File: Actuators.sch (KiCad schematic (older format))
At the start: 14 parts, among them J1 SERVO PWR, M1 Motor_Servo, M2 Motor_Servo, M3 Pump 1, M4 Pump 2, U6 DRV8847PWR

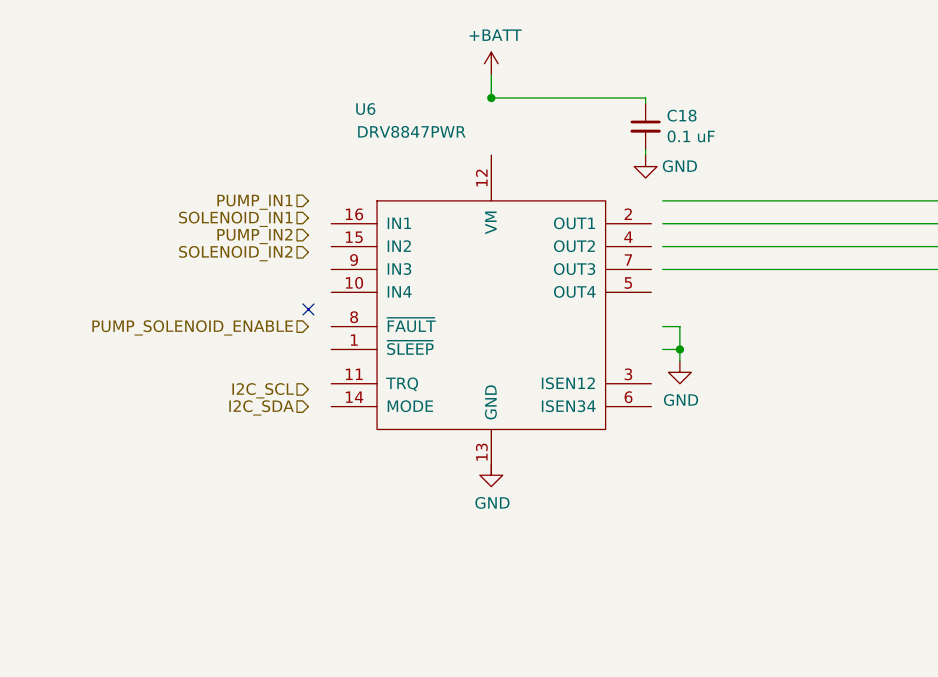
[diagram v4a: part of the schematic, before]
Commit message: Switch to SPI, fixed sensor and motor driver symbols.
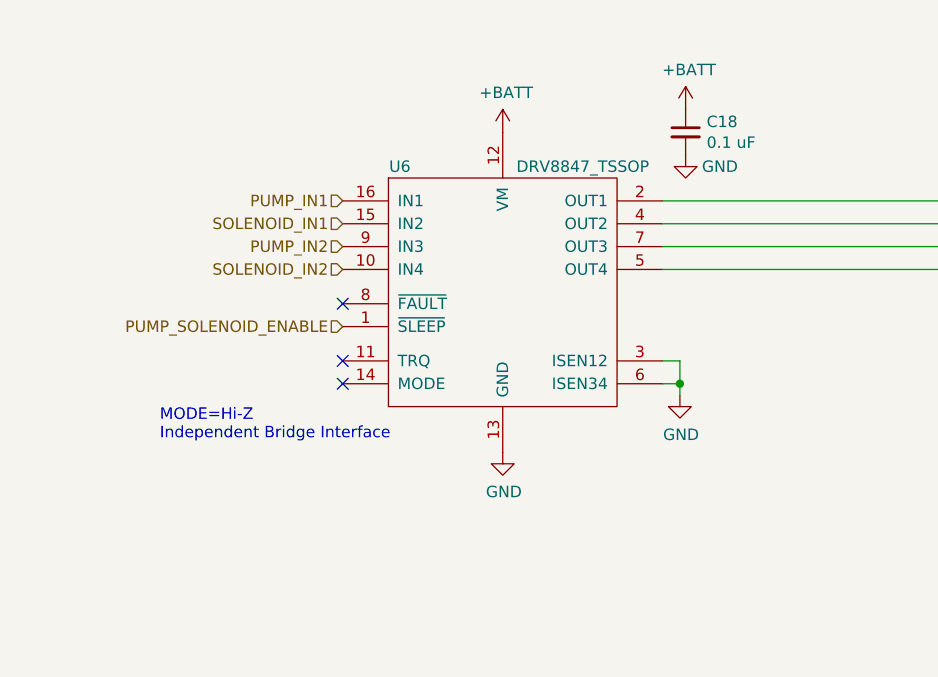
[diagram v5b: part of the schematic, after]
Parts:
- U6: value DRV8847PWR -> DRV8847_TSSOP; Digikey 296-53425-1-ND -> (none)
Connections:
- net labels removed: I2C_SCL, I2C_SDA
- wire segments 48 -> 44
- no-connect marks 1 -> 3
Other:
- note added: "MODE=Hi-Z\nIndependent Bridge Interface"
- moved on the sheet: C18
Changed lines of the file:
@@
 Comment4 ""
 $EndDescr
-Text HLabel 3700 2650 0    50   Input ~ 0
+Text HLabel 3850 2650 0    50   Input ~ 0
 PUMP_IN1
-Text HLabel 3700 2800 0    50   Input ~ 0
+Text HLabel 3850 2850 0    50   Input ~ 0
 PUMP_IN2
-Text HLabel 3700 3200 0    50   Input ~ 0
+Text HLabel 3850 3200 0    50   Input ~ 0
 PUMP_SOLENOID_ENABLE
 Text HLabel 4500 5250 0    50   Input ~ 0
@@
 Text HLabel 4500 5800 0    50   Input ~ 0
 SERVO2
-Text HLabel 3700 3550 0    50   Input ~ 0
-I2C_SDA
-Text HLabel 3700 3475 0    50   Input ~ 0
-I2C_SCL
-NoConn ~ 3700 3125
-$Comp
-L power:GND #PWR035
+NoConn ~ 3850 3100
+$Comp
+L power:GND #PWR037
 U 1 1 5E239CA6
-P 4500 3800
-F 0 "#PWR035" H 4500 3550 50  0001 C CNN
-F 1 "GND" H 4505 3627 50  0000 C CNN
-F 2 "" H 4500 3800 50  0001 C CNN
-F 3 "" H 4500 3800 50  0001 C CNN
-	1    4500 3800
-	1    0    0    -1
-$EndComp
-$Comp
-L power:GND #PWR039
+P 4550 3750
+F 0 "#PWR037" H 4550 3500 50  0001 C CNN
+F 1 "GND" H 4555 3577 50  0000 C CNN
+F 2 "" H 4550 3750 50  0001 C CNN
+F 3 "" H 4550 3750 50  0001 C CNN
+	1    4550 3750
+	1    0    0    -1
+$EndComp
+$Comp
+L power:GND #PWR040
 U 1 1 5E260916
-P 5325 3350
-F 0 "#PWR039" H 5325 3100 50  0001 C CNN
-F 1 "GND" H 5330 3177 50  0000 C CNN
-F 2 "" H 5325 3350 50  0001 C CNN
-F 3 "" H 5325 3350 50  0001 C CNN
-	1    5325 3350
-	1    0    0    -1
-$EndComp
-Wire Wire Line
-	5250 3300 5325 3300
-Wire Wire Line
-	5250 3200 5325 3200
-Wire Wire Line
-	5325 3200 5325 3300
-Connection ~ 5325 3300
-Wire Wire Line
-	5325 3300 5325 3350
-Text HLabel 3700 2875 0    50   Input ~ 0
+P 5325 3500
+F 0 "#PWR040" H 5325 3250 50  0001 C CNN
+F 1 "GND" H 5330 3327 50  0000 C CNN
+F 2 "" H 5325 3500 50  0001 C CNN
+F 3 "" H 5325 3500 50  0001 C CNN
+	1    5325 3500
+	1    0    0    -1
+$EndComp
+Wire Wire Line
+	5250 3450 5325 3450
+Wire Wire Line
+	5250 3350 5325 3350
+Wire Wire Line
+	5325 3350 5325 3450
+Connection ~ 5325 3450
+Wire Wire Line
+	5325 3450 5325 3500
+Text HLabel 3850 2950 0    50   Input ~ 0
 SOLENOID_IN2
-$Comp
-L Device:C_Small C18
-U 1 1 5E2FBBF2
-P 5175 2325
-F 0 "C18" H 5267 2371 50  0000 L CNN
-F 1 "0.1 uF" H 5267 2280 50  0000 L CNN
-F 2 "" H 5175 2325 50  0001 C CNN
-F 3 "~" H 5175 2325 50  0001 C CNN
-	1    5175 2325
-	1    0    0    -1
-$EndComp
-$Comp
-L power:GND #PWR038
-U 1 1 5E2FC82D
-P 5175 2450
-F 0 "#PWR038" H 5175 2200 50  0001 C CNN
-F 1 "GND" H 5325 2400 50  0000 C CNN
-F 2 "" H 5175 2450 50  0001 C CNN
-F 3 "" H 5175 2450 50  0001 C CNN
-	1    5175 2450
-	1    0    0    -1
-$EndComp
-Wire Wire Line
-	5175 2225 5175 2200
-Wire Wire Line
-	4500 2200 5175 2200
-Wire Wire Line
-	5175 2425 5175 2450
 $Comp
 L Motor:Motor_Servo M1
@@
 	1    0    0    -1
 $EndComp
-$Comp
-L _power:DRV8847_TSSOP U6
-U 1 1 5E23D2B5
-P 4500 3150
-F 0 "U6" H 3950 4050 50  0000 C CNN
-F 1 "DRV8847PWR" H 4150 3950 50  0000 C CNN
-F 2 "" H 4500 3150 50  0001 C CNN
-F 3 "" H 4500 3150 50  0001 C CNN
-F 4 "296-53425-1-ND" H 4500 3150 50  0001 C CNN "Digikey"
-	1    4500 3150
-	1    0    0    -1
-$EndComp
-Text HLabel 3700 2725 0    50   Input ~ 0
+Text HLabel 3850 2750 0    50   Input ~ 0
 SOLENOID_IN1
 $Comp
@@
 P 3350 5650
 AR Path="/5E3A79FB" Ref="#PWR?"  Part="1"
-AR Path="/5E1FB153/5E3A79FB" Ref="#PWR033"  Part="1"
-F 0 "#PWR033" H 3350 5400 50  0001 C CNN
+AR Path="/5E1FB153/5E3A79FB" Ref="#PWR035"  Part="1"
+F 0 "#PWR035" H 3350 5400 50  0001 C CNN
 F 1 "GND" H 3355 5477 50  0000 C CNN
 F 2 "" H 3350 5650 50  0001 C CNN
@@
 P 4700 5450
 AR Path="/5E3D17A5" Ref="#PWR?"  Part="1"
-AR Path="/5E1FB153/5E3D17A5" Ref="#PWR036"  Part="1"
-F 0 "#PWR036" H 4700 5200 50  0001 C CNN
+AR Path="/5E1FB153/5E3D17A5" Ref="#PWR038"  Part="1"
+F 0 "#PWR038" H 4700 5200 50  0001 C CNN
 F 1 "GND" H 4705 5277 50  0000 C CNN
 F 2 "" H 4700 5450 50  0001 C CNN
@@
 P 4700 6000
 AR Path="/5E3D4696" Ref="#PWR?"  Part="1"
-AR Path="/5E1FB153/5E3D4696" Ref="#PWR037"  Part="1"
-F 0 "#PWR037" H 4700 5750 50  0001 C CNN
+AR Path="/5E1FB153/5E3D4696" Ref="#PWR039"  Part="1"
+F 0 "#PWR039" H 4700 5750 50  0001 C CNN
 F 1 "GND" H 4705 5827 50  0000 C CNN
 F 2 "" H 4700 6000 50  0001 C CNN
@@
 	4700 5250 4500 5250
 $Comp
-L power:+BATT #PWR034
+L power:+BATT #PWR036
 U 1 1 5E3DDDE9
-P 4500 2100
-F 0 "#PWR034" H 4500 1950 50  0001 C CNN
-F 1 "+BATT" H 4515 2273 50  0000 C CNN
-F 2 "" H 4500 2100 50  0001 C CNN
-F 3 "" H 4500 2100 50  0001 C CNN
-	1    4500 2100
-	1    0    0    -1
-$EndComp
-Wire Wire Line
-	4500 2200 4500 2100
-Connection ~ 4500 2200
+P 4550 2350
+F 0 "#PWR036" H 4550 2200 50  0001 C CNN
+F 1 "+BATT" H 4565 2523 50  0000 C CNN
+F 2 "" H 4550 2350 50  0001 C CNN
+F 3 "" H 4550 2350 50  0001 C CNN
+	1    4550 2350
+	1    0    0    -1
+$EndComp
 $Comp
 L Motor:Motor_DC M3
@@
 Text Notes 7600 4250 0    50   ~ 0
 Actuator 2\n(1A max)
+$Comp
+L _power:DRV8847_TSSOP U6
+U 1 1 5E3FBC0B
+P 4550 3050
+F 0 "U6" H 4100 3600 50  0000 C CNN
+F 1 "DRV8847_TSSOP" H 4900 3600 50  0000 C CNN
+F 2 "" H 4550 3000 50  0001 C CNN
+F 3 "http://www.ti.com/lit/ds/symlink/drv8847.pdf" H 4550 3000 50  0001 C CNN
+	1    4550 3050
+	1    0    0    -1
+$EndComp
+$Comp
+L power:GND #PWR041
+U 1 1 5E2FC82D
+P 5350 2450
+F 0 "#PWR041" H 5350 2200 50  0001 C CNN
+F 1 "GND" H 5500 2400 50  0000 C CNN
+F 2 "" H 5350 2450 50  0001 C CNN
+F 3 "" H 5350 2450 50  0001 C CNN
+	1    5350 2450
+	1    0    0    -1
+$EndComp
+$Comp
+L Device:C_Small C18
+U 1 1 5E2FBBF2
+P 5350 2350
+F 0 "C18" H 5442 2396 50  0000 L CNN
+F 1 "0.1 uF" H 5442 2305 50  0000 L CNN
+F 2 "" H 5350 2350 50  0001 C CNN
+F 3 "~" H 5350 2350 50  0001 C CNN
+	1    5350 2350
+	1    0    0    -1
+$EndComp
+NoConn ~ 3850 3450
+NoConn ~ 3850 3350
+Text Notes 3050 3700 0    50   ~ 0
+MODE=Hi-Z\nIndependent Bridge Interface
+$Comp
+L power:+BATT #PWR?
+U 1 1 5E4403AD
+P 5350 2250
+F 0 "#PWR?" H 5350 2100 50  0001 C CNN
+F 1 "+BATT" H 5365 2423 50  0000 C CNN
+F 2 "" H 5350 2250 50  0001 C CNN
+F 3 "" H 5350 2250 50  0001 C CNN
+	1    5350 2250
+	1    0    0    -1
+$EndComp
 $EndSCHEMATC

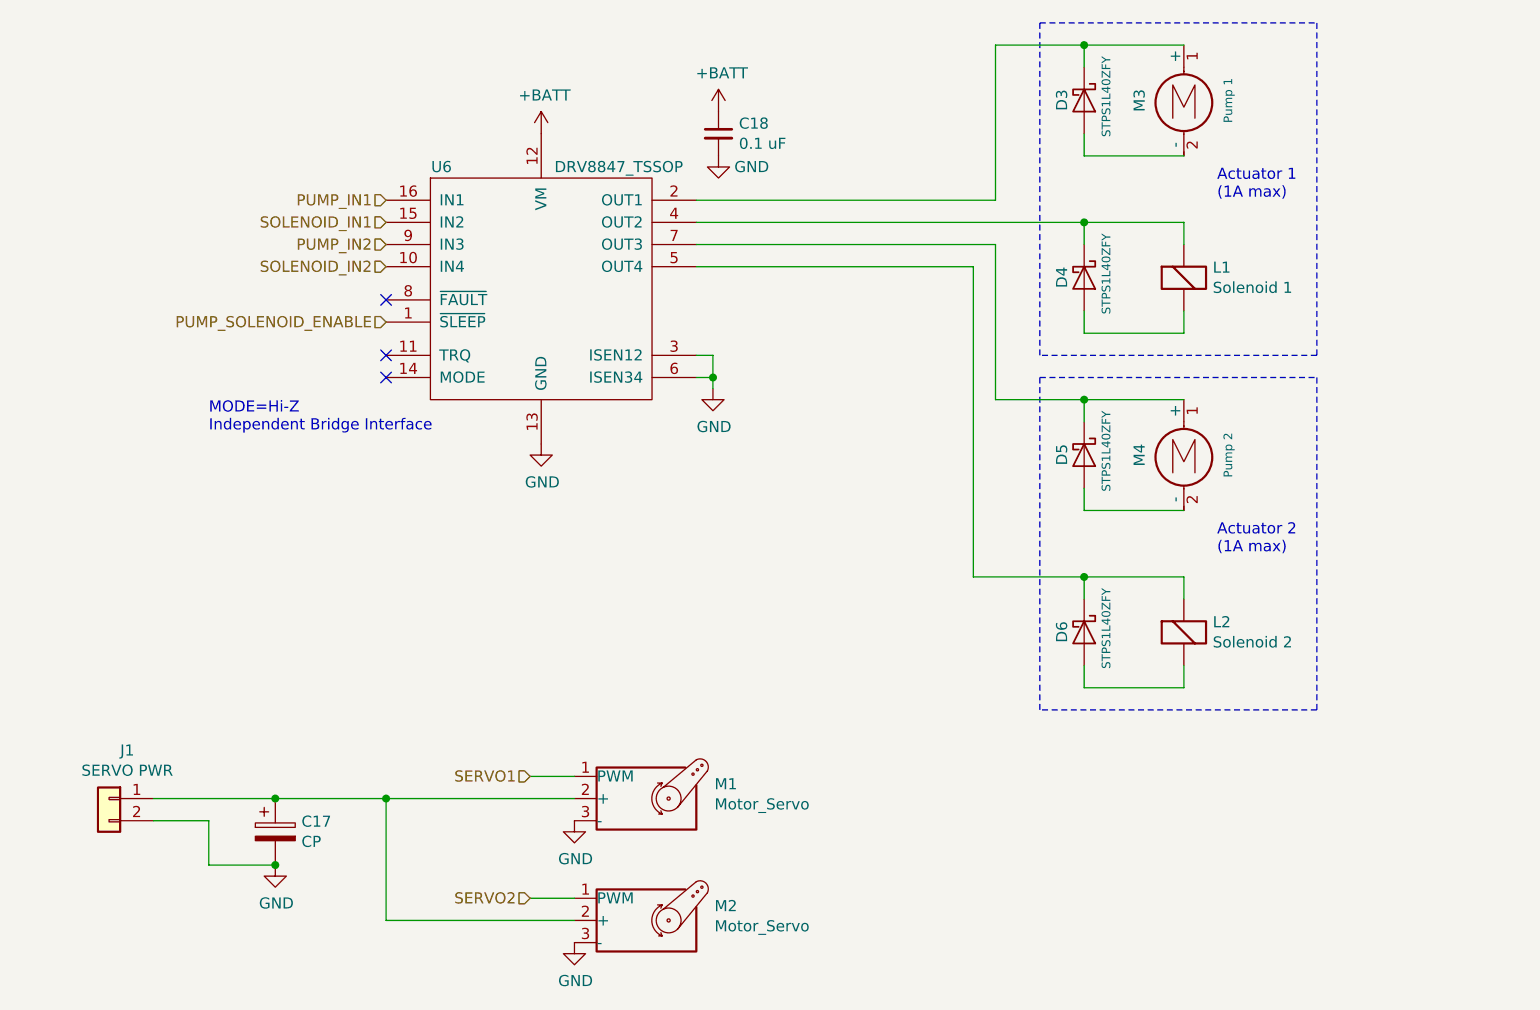
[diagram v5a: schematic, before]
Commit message: Work on footprint assignment
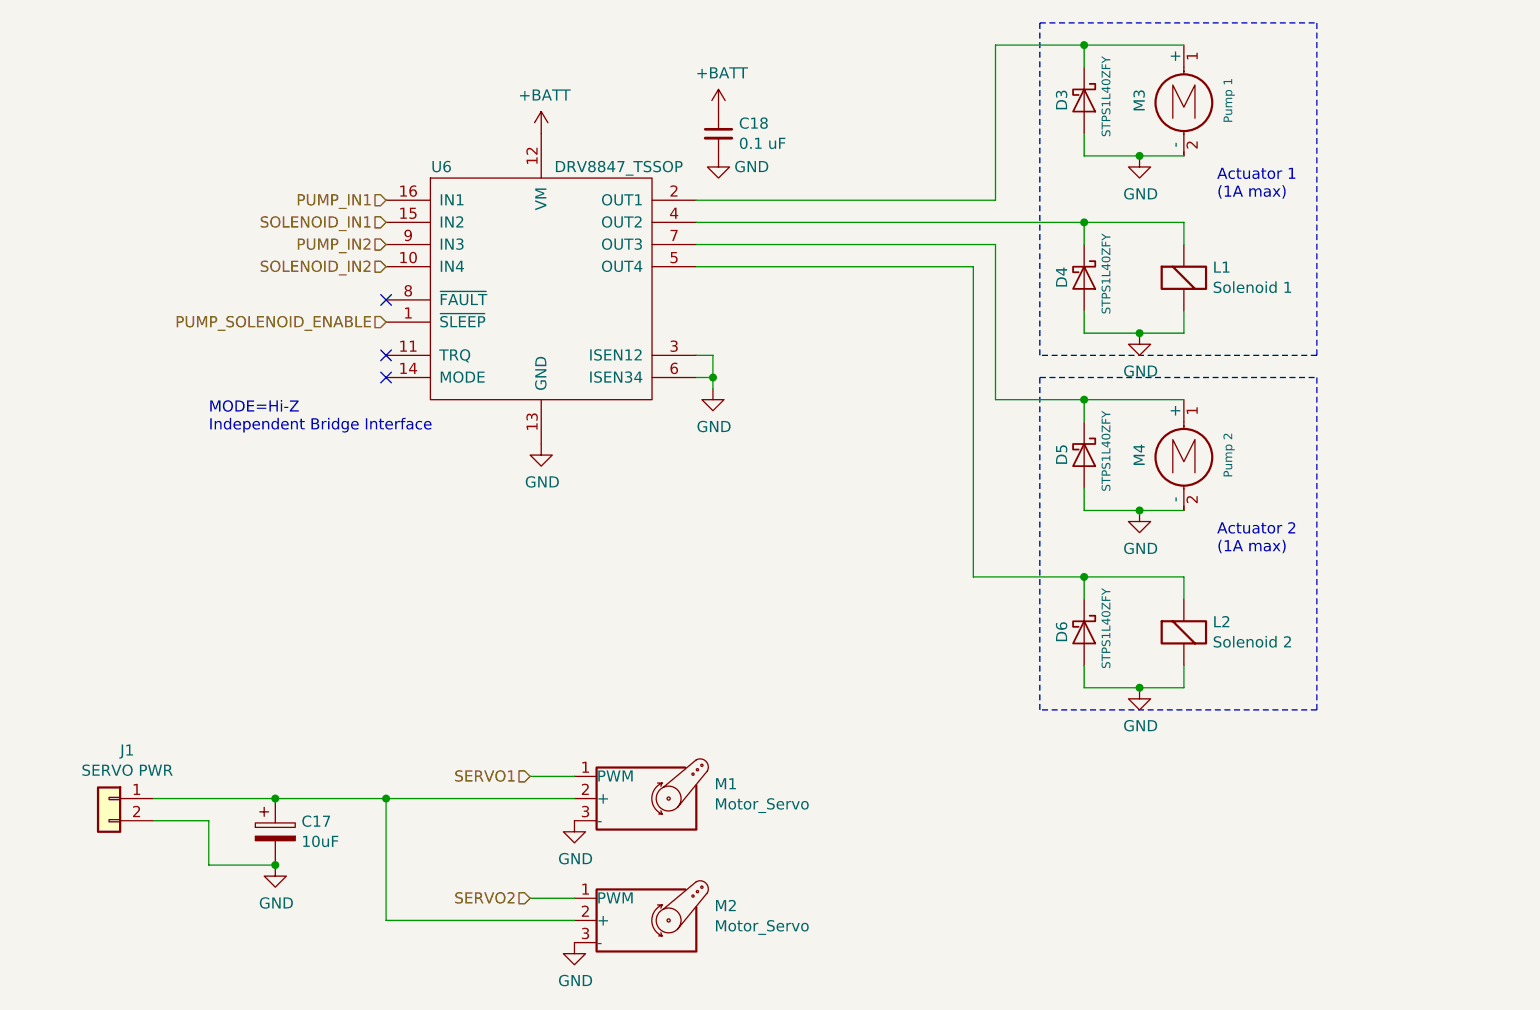
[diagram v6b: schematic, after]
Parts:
- C17: value CP -> 10uF
- C18: footprint (none) -> Capacitor_SMD:C_0603_1608Metric
- M1, M2: footprint (none) -> Connector_PinHeader_2.54mm:PinHeader_1x03_P2.54mm_Horizontal
- U6: footprint (none) -> Package_SO:TSSOP-16_4.4x5mm_P0.65mm
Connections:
- net GND: now also D3.2 (A), D4.2 (A), D5.2 (A), D6.2 (A), L1.2 (+), L2.2 (+), M3.2 (-), M4.2 (-)
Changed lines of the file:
@@
 F 0 "M1" H 5332 5415 50  0000 L CNN
 F 1 "Motor_Servo" H 5332 5324 50  0000 L CNN
-F 2 "" H 5000 5160 50  0001 C CNN
+F 2 "Connector_PinHeader_2.54mm:PinHeader_1x03_P2.54mm_Horizontal" H 5000 5160 50  0001 C CNN
 F 3 "http://forums.parallax.com/uploads/attachments/46831/74481.png" H 5000 5160 50  0001 C CNN
 	1    5000 5350
@@
 F 0 "M2" H 5332 5965 50  0000 L CNN
 F 1 "Motor_Servo" H 5332 5874 50  0000 L CNN
-F 2 "" H 5000 5710 50  0001 C CNN
+F 2 "Connector_PinHeader_2.54mm:PinHeader_1x03_P2.54mm_Horizontal" H 5000 5710 50  0001 C CNN
 F 3 "http://forums.parallax.com/uploads/attachments/46831/74481.png" H 5000 5710 50  0001 C CNN
 	1    5000 5900
@@
 AR Path="/5E1FB153/5E3A79F5" Ref="C17"  Part="1"
 F 0 "C17" H 3468 5546 50  0000 L CNN
-F 1 "CP" H 3468 5455 50  0000 L CNN
+F 1 "10uF" H 3468 5455 50  0000 L CNN
 F 2 "" H 3388 5350 50  0001 C CNN
 F 3 "~" H 3350 5500 50  0001 C CNN
@@
 	7000 2350 7000 2450
 Wire Wire Line
-	7000 2450 7450 2450
+	7000 2450 7250 2450
 Wire Wire Line
 	7000 3650 7000 3550
@@
 	7000 3950 7000 4050
 Wire Wire Line
-	7000 4050 7450 4050
+	7000 4050 7250 4050
 Wire Wire Line
 	7000 4450 7000 4350
@@
 	7000 4750 7000 4850
 Wire Wire Line
-	7000 4850 7450 4850
+	7000 4850 7250 4850
 $Comp
 L Device:D_Schottky D3
@@
 	7000 3150 7000 3250
 Wire Wire Line
-	7000 3250 7450 3250
-Wire Wire Line
 	7000 2750 7450 2750
 Wire Wire Line
@@
 F 0 "U6" H 4100 3600 50  0000 C CNN
 F 1 "DRV8847_TSSOP" H 4900 3600 50  0000 C CNN
-F 2 "" H 4550 3000 50  0001 C CNN
+F 2 "Package_SO:TSSOP-16_4.4x5mm_P0.65mm" H 4550 3000 50  0001 C CNN
 F 3 "http://www.ti.com/lit/ds/symlink/drv8847.pdf" H 4550 3000 50  0001 C CNN
 	1    4550 3050
@@
 F 0 "C18" H 5442 2396 50  0000 L CNN
 F 1 "0.1 uF" H 5442 2305 50  0000 L CNN
-F 2 "" H 5350 2350 50  0001 C CNN
+F 2 "Capacitor_SMD:C_0603_1608Metric" H 5350 2350 50  0001 C CNN
 F 3 "~" H 5350 2350 50  0001 C CNN
 	1    5350 2350
@@
 MODE=Hi-Z\nIndependent Bridge Interface
 $Comp
-L power:+BATT #PWR?
+L power:+BATT #PWR0101
 U 1 1 5E4403AD
 P 5350 2250
-F 0 "#PWR?" H 5350 2100 50  0001 C CNN
+F 0 "#PWR0101" H 5350 2100 50  0001 C CNN
 F 1 "+BATT" H 5365 2423 50  0000 C CNN
 F 2 "" H 5350 2250 50  0001 C CNN
@@
 	1    0    0    -1
 $EndComp
+$Comp
+L power:GND #PWR0102
+U 1 1 5E3F7C81
+P 7250 2450
+F 0 "#PWR0102" H 7250 2200 50  0001 C CNN
+F 1 "GND" H 7255 2277 50  0000 C CNN
+F 2 "" H 7250 2450 50  0001 C CNN
+F 3 "" H 7250 2450 50  0001 C CNN
+	1    7250 2450
+	1    0    0    -1
+$EndComp
+Connection ~ 7250 2450
+Wire Wire Line
+	7250 2450 7450 2450
+Wire Wire Line
+	7000 3250 7250 3250
+$Comp
+L power:GND #PWR0103
+U 1 1 5E3F96C2
+P 7250 3250
+F 0 "#PWR0103" H 7250 3000 50  0001 C CNN
+F 1 "GND" H 7255 3077 50  0000 C CNN
+F 2 "" H 7250 3250 50  0001 C CNN
+F 3 "" H 7250 3250 50  0001 C CNN
+	1    7250 3250
+	1    0    0    -1
+$EndComp
+Connection ~ 7250 3250
+Wire Wire Line
+	7250 3250 7450 3250
+$Comp
+L power:GND #PWR0104
+U 1 1 5E3F9BB4
+P 7250 4050
+F 0 "#PWR0104" H 7250 3800 50  0001 C CNN
+F 1 "GND" H 7255 3877 50  0000 C CNN
+F 2 "" H 7250 4050 50  0001 C CNN
+F 3 "" H 7250 4050 50  0001 C CNN
+	1    7250 4050
+	1    0    0    -1
+$EndComp
+Connection ~ 7250 4050
+Wire Wire Line
+	7250 4050 7450 4050
+$Comp
+L power:GND #PWR0105
+U 1 1 5E3FA1D8
+P 7250 4850
+F 0 "#PWR0105" H 7250 4600 50  0001 C CNN
+F 1 "GND" H 7255 4677 50  0000 C CNN
+F 2 "" H 7250 4850 50  0001 C CNN
+F 3 "" H 7250 4850 50  0001 C CNN
+	1    7250 4850
+	1    0    0    -1
+$EndComp
+Connection ~ 7250 4850
+Wire Wire Line
+	7250 4850 7450 4850
 $EndSCHEMATC

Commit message: Review update
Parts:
- added C19: 22uF, symbol Device:CP
- added R2: 10k, symbol Device:R_Small
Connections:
- net +BATT: now also C19.1
- net GND: now also U6.11 (TRQ), C19.2, R2.2
- net PUMP_SOLENOID_ENABLE: now also R2.1
- no-connect marks 3 -> 2
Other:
- note added: "MODE=Hi-Z: Independent Bridge Interface\nTRQ=0: Full current"
- note added: "≥16V"
- note removed: "MODE=Hi-Z\nIndependent Bridge Interface"
- moved on the sheet: C18, D5, D6, L2, M4

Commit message: Input range note, rough footprint assignment
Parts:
- C17: footprint (none) -> Capacitor_SMD:C_1206_3216Metric
- C19: footprint (none) -> Capacitor_THT:CP_Radial_D6.3mm_P2.50mm
- J1, L1, L2, M3, M4: footprint (none) -> Connector_PinHeader_2.54mm:PinHeader_1x02_P2.54mm_Vertical
- R2: footprint (none) -> Resistor_SMD:R_0603_1608Metric
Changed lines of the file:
@@
 F 0 "C17" H 3468 5546 50  0000 L CNN
 F 1 "10uF" H 3468 5455 50  0000 L CNN
-F 2 "" H 3388 5350 50  0001 C CNN
+F 2 "Capacitor_SMD:C_1206_3216Metric" H 3388 5350 50  0001 C CNN
 F 3 "~" H 3350 5500 50  0001 C CNN
 	1    3350 5500
@@
 F 0 "J1" H 2518 5567 50  0000 C CNN
 F 1 "SERVO PWR" H 2518 5476 50  0000 C CNN
-F 2 "" H 2600 5350 50  0001 C CNN
+F 2 "Connector_PinHeader_2.54mm:PinHeader_1x02_P2.54mm_Vertical" H 2600 5350 50  0001 C CNN
 F 3 "~" H 2600 5350 50  0001 C CNN
 	1    2600 5350
@@
 F 0 "M3" V 7250 2100 50  0000 C CNN
 F 1 "Pump 1" V 7650 2100 39  0000 C CNN
-F 2 "" H 7450 2060 50  0001 C CNN
+F 2 "Connector_PinHeader_2.54mm:PinHeader_1x02_P2.54mm_Vertical" H 7450 2060 50  0001 C CNN
 F 3 "~" H 7450 2060 50  0001 C CNN
 	1    7450 2150
@@
 F 0 "M4" V 7250 3850 50  0000 C CNN
 F 1 "Pump 2" V 7650 3850 39  0000 C CNN
-F 2 "" H 7450 3810 50  0001 C CNN
+F 2 "Connector_PinHeader_2.54mm:PinHeader_1x02_P2.54mm_Vertical" H 7450 3810 50  0001 C CNN
 F 3 "~" H 7450 3810 50  0001 C CNN
 	1    7450 3900
@@
 F 0 "L1" H 7580 3146 50  0000 L CNN
 F 1 "Solenoid 1" H 7580 3055 50  0000 L CNN
-F 2 "" V 7425 3150 50  0001 C CNN
+F 2 "Connector_PinHeader_2.54mm:PinHeader_1x02_P2.54mm_Vertical" V 7425 3150 50  0001 C CNN
 F 3 "~" V 7425 3150 50  0001 C CNN
 	1    7450 3050
@@
 F 0 "L2" H 7580 4896 50  0000 L CNN
 F 1 "Solenoid 2" H 7580 4805 50  0000 L CNN
-F 2 "" V 7425 4900 50  0001 C CNN
+F 2 "Connector_PinHeader_2.54mm:PinHeader_1x02_P2.54mm_Vertical" V 7425 4900 50  0001 C CNN
 F 3 "~" V 7425 4900 50  0001 C CNN
 	1    7450 4800
@@
 F 0 "C19" H 5200 2250 50  0000 L CNN
 F 1 "22uF" H 5200 2150 50  0000 L CNN
-F 2 "" H 5538 2050 50  0001 C CNN
+F 2 "Capacitor_THT:CP_Radial_D6.3mm_P2.50mm" H 5538 2050 50  0001 C CNN
 F 3 "~" H 5500 2200 50  0001 C CNN
 	1    5500 2200
@@
 F 0 "R2" H 3459 3346 50  0000 L CNN
 F 1 "10k" H 3459 3255 50  0000 L CNN
-F 2 "" H 3400 3300 50  0001 C CNN
+F 2 "Resistor_SMD:R_0603_1608Metric" H 3400 3300 50  0001 C CNN
 F 3 "~" H 3400 3300 50  0001 C CNN
 	1    3400 3300
